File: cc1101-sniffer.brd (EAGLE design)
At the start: 52 x 28 mm, 43 parts, among them J1 USB4105-GF-A, J2 61300411821, U1 AP2112K, U2 RP2040, U3 W25Q32JVSSIQ, Y1 ABM8G-12.000MHZ-18-D2Y-T3

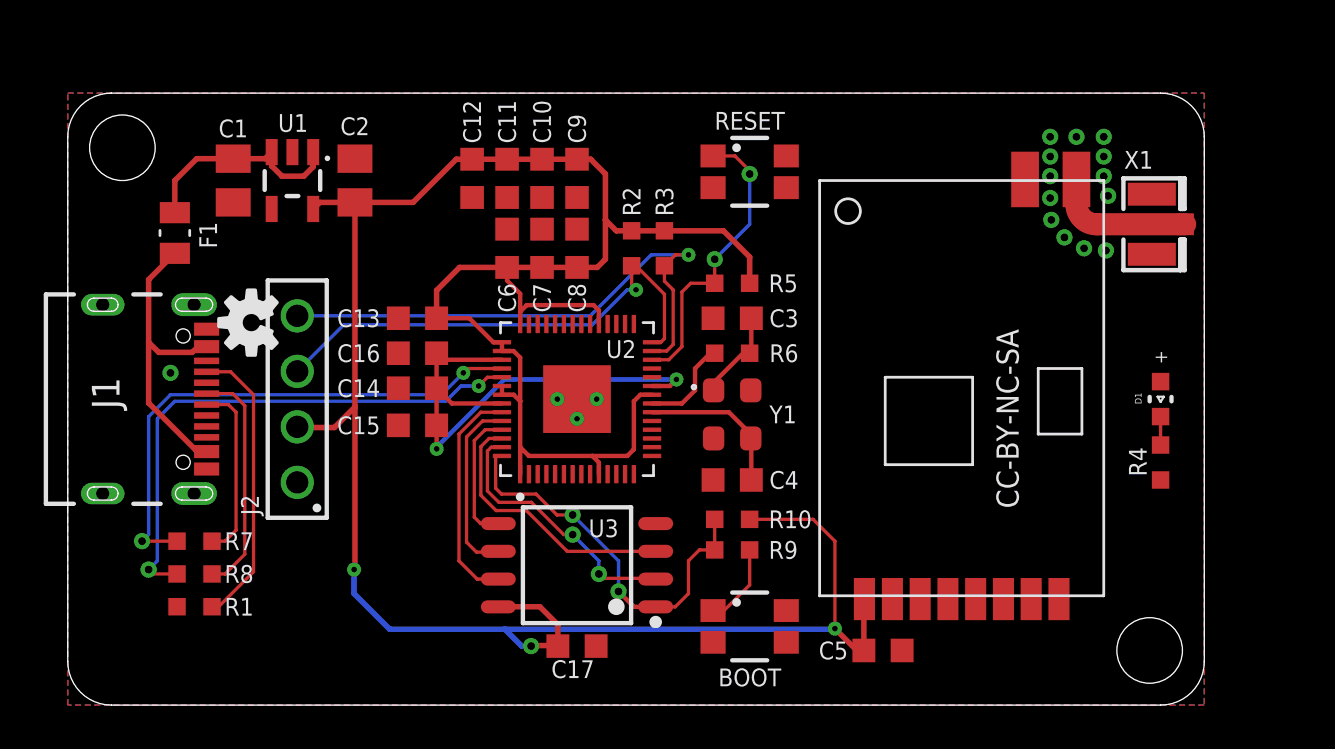
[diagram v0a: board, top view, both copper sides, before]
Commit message: tCream for USB and E01-900M10S
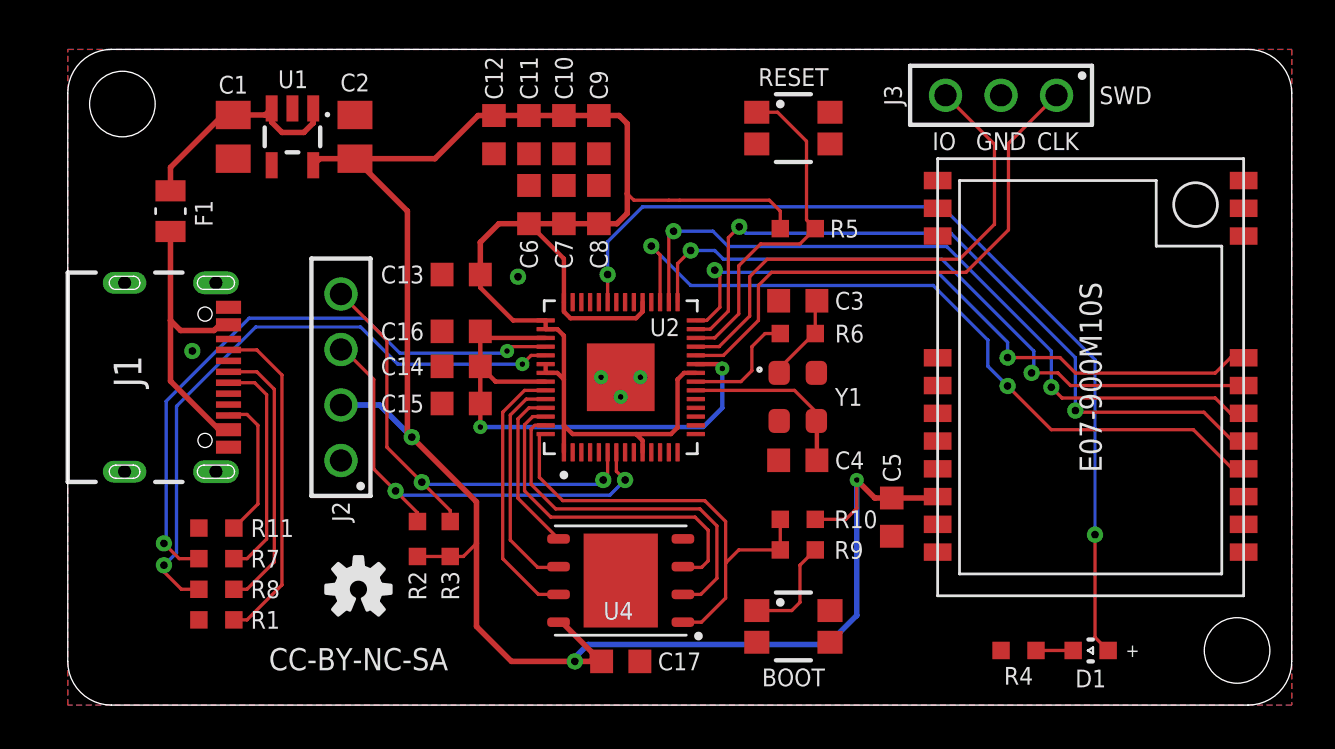
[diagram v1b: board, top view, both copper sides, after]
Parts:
- removed U$2: CC1101-868MS10, codm:CC1101-868MS10
- removed U3: W25Q32JVSSIQ, W25Q32JVSSIQ:SOIC127P790X216-8N
- removed X1: (no value), adafruit:U.FL
- added J3: 61300311821, Eagle_WR-PHD (rev21a):61300311821
- added R11: 5k1, codm:R0603RF
- added U$6: E07-900M10S, codm:E07-900M10S
- added U4: W25Q32JVZPIQ, W25Q32JVZPIQ:SON127P600X500X80-9N
- moved U$5 17.0 mm to (47.0, 22.5)
- moved R2 16.5 mm to (16.0, 7.60), turned to 270 degrees
- moved R3 16.5 mm to (17.5, 7.60), turned to 270 degrees
- moved U$4 13.1 mm to (13.3, 5.30), turned to 0 degrees
- moved D1 11.9 mm to (46.8, 2.50), turned to 0 degrees
- moved R4 10.8 mm to (43.5, 2.50), turned to 0 degrees
- moved U$3 8.06 mm to (43.2, 11.3)
- moved C5 6.11 mm to (37.7, 8.60), turned to 90 degrees
- moved R5 3.91 mm to (33.4, 21.8), turned to 0 degrees
- moved C4 3.13 mm to (33.4, 11.2)
- moved R6 3.13 mm to (33.4, 17.0)
- moved C3 3.10 mm to (33.4, 18.5)
- moved Y1 3.10 mm to (33.4, 14.1)
- moved R10 3.00 mm to (33.4, 8.50)
- moved R9 3.00 mm to (33.4, 7.10)
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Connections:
- removed net N$5: U$2.ANT, X1.3
- new net N$9: J1.B5, R11.2
- new net SWCLK: J3.1, U2.24
- new net SWD: J3.3, U2.25
- net +3V3: now also U$6.9, U4.8; no longer U$2.VCC, U3.8
- net CSN: now also U$6.19, U2.28; no longer U$2.CSN
- net GDO0: now also U$6.15, U2.31; no longer U$2.GDO0
- net GND: now also J3.2, R11.1, U$6.1, U$6.11, U$6.12, U$6.2, U$6.20, U$6.22, U$6.3, U$6.4, U$6.5, U4.4; no longer U$2.GND@0, U$2.GND@1, U3.4, X1.1, X1.2
- net LED0: now also U2.37
- net MISO: now also U$6.16, U2.27; no longer U$2.MISO
- net MOSI: now also U$6.17, U2.30; no longer U$2.MOSI
- net QSPI_CSN: now also U4.1; no longer U3.1
- net QSPI_SCLK: now also U4.6; no longer U3.6
- net QSPI_SD0: now also U4.5; no longer U3.5
- net QSPI_SD1: now also U4.2; no longer U3.2
- net QSPI_SD2: now also U4.3; no longer U3.3
- net QSPI_SD3: now also U4.7; no longer U3.7
- net SCL: now also U2.7; no longer U2.28
- net SCLK: now also U$6.18, U2.29; no longer U$2.SCK
- net SDA: now also U2.6; no longer U2.27
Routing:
- net LED0: track 0.00 -> 42.2 mm, vias 0 -> 2
- net GDO0: track 0.00 -> 34.8 mm, vias 0 -> 2
- net MISO: track 0.00 -> 34.5 mm, vias 0 -> 2
- net MOSI: track 0.00 -> 33.8 mm, vias 0 -> 2
- net SCLK: track 0.00 -> 31.2 mm, vias 0 -> 2
- net CSN: track 0.00 -> 30.0 mm, vias 0 -> 2
- net SWCLK: track 0.00 -> 24.7 mm
- net SWD: track 0.00 -> 23.9 mm
- net N$9: track 0.00 -> 6.73 mm
- net N$5: track 6.49 -> 0.00 mm
- net +3V3: track 127.9 -> 134.3 mm
- net QSPI_SD1: track 12.4 -> 16.8 mm, vias 2 -> 0
- net N$4: track 25.0 -> 29.0 mm
- net N$8: track 24.5 -> 28.2 mm
- net QSPI_SD2: track 12.4 -> 16.0 mm
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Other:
- board size 52 x 28 mm -> 56 x 30 mm
- board text added: "90510-0.2 codm.de, 2022"
- board text added: "CC1101 Sniffer V0.2 codm.de, 2022"
- board text added: "CLK"
- board text added: "IO"
- board text added: "SWD"
- board text added: "Thanks to jp112sdl, psi-4ward, TomMajor, pa-pa"
- board text removed: "90510-0.1 codm.de, 2022"
